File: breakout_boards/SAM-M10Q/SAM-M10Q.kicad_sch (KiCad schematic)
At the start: 10 parts, among them J1 Conn_01x06_Pin, U1 SAM-M10Q

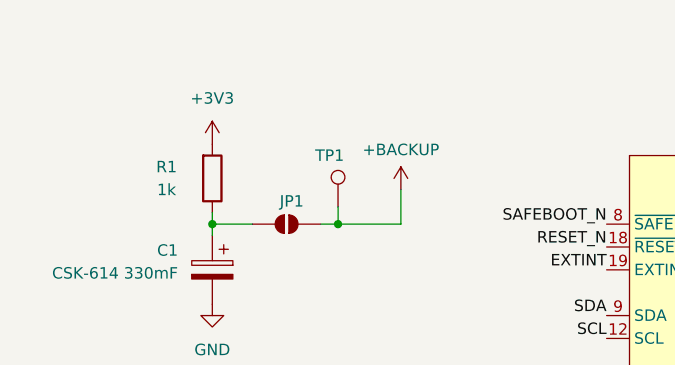
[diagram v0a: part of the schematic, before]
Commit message: made new M10Q footprint and added a diode
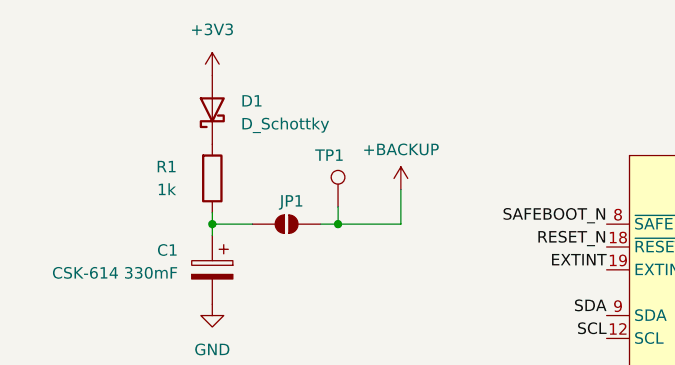
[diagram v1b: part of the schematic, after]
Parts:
- added D1: D_Schottky, symbol Device:D_Schottky
- J1: footprint _footprints:PinHeader_1x06_P2.54mm_Vertical_SMD_Pin1Left -> _footprints:JST_XH_1x06_P2.54mm_Horizontal
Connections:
- net +3V3: now also D1.2 (A); no longer R1.2
- new net: D1.1 (K), R1.2
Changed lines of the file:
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@@
 			)
 		)
-		(property "Footprint" "_footprints:PinHeader_1x06_P2.54mm_Vertical_SMD_Pin1Left"
+		(property "Footprint" "_footprints:JST_XH_1x06_P2.54mm_Horizontal"
 			(at 252.73 88.265 0)
 			(effects
@@
 	(symbol
 		(lib_id "power:+3V3")
-		(at 75.565 76.835 0)
+		(at 75.565 69.215 0)
 		(mirror y)
 		(unit 1)
@@
 		(fields_autoplaced yes)
 		(property "Reference" "#PWR07"
-			(at 75.565 80.645 0)
+			(at 75.565 73.025 0)
 			(effects
 				(font
@@
 		)
 		(property "Value" "+3V3"
-			(at 75.565 71.755 0)
+			(at 75.565 64.135 0)
 			(effects
 				(font
@@
 		)
 		(property "Footprint" ""
-			(at 75.565 76.835 0)
+			(at 75.565 69.215 0)
 			(effects
 				(font
@@
 		)
 		(property "Datasheet" ""
-			(at 75.565 76.835 0)
+			(at 75.565 69.215 0)
 			(effects
 				(font
@@
 		)
 		(property "Description" "Power symbol creates a global label with name \"+3V3\""
-			(at 75.565 76.835 0)
+			(at 75.565 69.215 0)
 			(effects
 				(font
@@
 					(unit 1)
 				)
+			)
+		)
+	)
+	(symbol
+		(lib_id "Device:D_Schottky")
+		(at 75.565 73.025 90)
+		(unit 1)
+		(exclude_from_sim no)
+		(in_bom yes)
+		(on_board yes)
+		(dnp no)
+		(fields_autoplaced yes)
+		(property "Reference" "D1"
+			(at 78.74 72.0724 90)
+			(effects
+				(font
+					(size 1.27 1.27)
+				)
+				(justify right)
+			)
+		)
+		(property "Value" "D_Schottky"
+			(at 78.74 74.6124 90)
+			(effects
+				(font
+					(size 1.27 1.27)
+				)
+				(justify right)
+			)
+		)
+		(property "Footprint" ""
+			(at 75.565 73.025 0)
+			(effects
+				(font
+					(size 1.27 1.27)
+				)
+				(hide yes)
+			)
+		)
+		(property "Datasheet" "~"
+			(at 75.565 73.025 0)
+			(effects
+				(font
+					(size 1.27 1.27)
+				)
+				(hide yes)
+			)
+		)
+		(property "Description" "Schottky diode"
+			(at 75.565 73.025 0)
+			(effects
+				(font
+					(size 1.27 1.27)
+				)
+				(hide yes)
+			)
+		)
+		(pin "1"
+		)
+		(pin "2"
+		)
+		(instances
+			(project ""
+				(path "/78205262-1082-4922-822c-8ba8bd5f39f9"
+					(reference "D1")
+					(unit 1)
+				)
